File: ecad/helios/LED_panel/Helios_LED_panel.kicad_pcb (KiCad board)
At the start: 2 copper layers, 100 x 102.5 mm, 29 parts

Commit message: Layouts and polishes the LED panel
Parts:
- removed D17, D18: White 4000K 3W, FORT:OSRAM_Platinium_Dragon_Reflector
- removed the REF** at (197.5, 60.0)
- removed the REF** at (127.5, 60.0)
- removed the REF** at (162.5, 95.0)
- removed the REF** at (127.5, 130.0)
- removed the REF** at (197.5, 130.0)
- added REF**: Carclo_10740, FORT:Carclo_10740, F.Cu at (132.5, 72.5)
- added REF**: Carclo_10740, FORT:Carclo_10740, F.Cu at (182.5, 122.5)
- added REF**: Carclo_10740, FORT:Carclo_10740, F.Cu at (207.5, 122.5)
- added REF**: Carclo_10740, FORT:Carclo_10740, F.Cu at (132.5, 147.5)
- added REF**: Carclo_10740, FORT:Carclo_10740, F.Cu at (157.5, 147.5)
- added REF**: Carclo_10740, FORT:Carclo_10740, F.Cu at (182.5, 147.5)
- added REF**: Carclo_10740, FORT:Carclo_10740, F.Cu at (207.5, 147.5)
- added REF**: Carclo_10740, FORT:Carclo_10740, F.Cu at (207.5, 97.5)
- added REF**: MountingHole_3.2mm_M3_DIN965, Mounting_Holes:MountingHole_3.2mm_M3_DIN965, F.Cu at (195.0, 85.0)
- added REF**: MountingHole_3.2mm_M3_DIN965, Mounting_Holes:MountingHole_3.2mm_M3_DIN965, F.Cu at (145.0, 85.0)
- added REF**: MountingHole_3.2mm_M3_DIN965, Mounting_Holes:MountingHole_3.2mm_M3_DIN965, F.Cu at (145.0, 135.0)
- added REF**: Carclo_10740, FORT:Carclo_10740, F.Cu at (157.5, 72.5)
- added REF**: MountingHole_3.2mm_M3_DIN965, Mounting_Holes:MountingHole_3.2mm_M3_DIN965, F.Cu at (195.0, 135.0)
- added REF**: Carclo_10740, FORT:Carclo_10740, F.Cu at (182.5, 72.5)
- added REF**: Carclo_10740, FORT:Carclo_10740, F.Cu at (207.5, 72.5)
- added REF**: Carclo_10740, FORT:Carclo_10740, F.Cu at (132.5, 97.5)
- added REF**: Carclo_10740, FORT:Carclo_10740, F.Cu at (157.5, 97.5)
- added REF**: Carclo_10740, FORT:Carclo_10740, F.Cu at (182.5, 97.5)
- added REF**: Carclo_10740, FORT:Carclo_10740, F.Cu at (132.5, 122.5)
- added REF**: Carclo_10740, FORT:Carclo_10740, F.Cu at (157.5, 122.5)
- D1, D10, D11, D12, D15, D16, D2, D3, D4, D5, D6, D7, D8, D9: footprint FORT:OSRAM_Platinium_Dragon_Reflector -> FORT:OSRAM_Platinium_Dragon
- D13, D14: value NIR 850nm 3W -> White 4000K 3W; footprint FORT:OSRAM_Platinium_Dragon_Reflector -> FORT:OSRAM_Platinium_Dragon
- moved IR_A_GND1 145.9 mm to (163.2, 63.2)
- moved D6 117.3 mm to (157.5, 147.5), turned to 270 degrees
- moved D15 107.4 mm to (207.5, 147.3)
- moved IR_B_VCC1 100.6 mm to (182.5, 63.2)
- moved D12 86.1 mm to (182.5, 147.5), turned to 270 degrees
- moved VIS_GND1 79.6 mm to (126.8, 63.2)
- moved D14 73.8 mm to (132.5, 147.5), turned to 270 degrees
- moved IR_B_GND1 70.3 mm to (177.0, 63.2)
- moved D5 66.4 mm to (157.5, 122.5), turned to 270 degrees
- moved D9 62.5 mm to (207.5, 97.5)
- moved D7 55.2 mm to (182.5, 72.5), turned to 270 degrees
- moved IR_A_VCC1 54.0 mm to (157.5, 63.2)
- moved D13 50.0 mm to (132.5, 72.5), turned to 270 degrees
- moved D1 49.1 mm to (157.5, 72.5)
- moved D2 47.6 mm to (157.5, 97.5)
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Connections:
- D13 pad 2: Net-(D12-Pad1) -> Net-(D13-Pad2)
- D15 pad 2: Net-(D15-Pad2) -> Net-(D14-Pad1)
- D7 pad 2: Net-(D6-Pad1) -> Net-(D7-Pad2)
- D8 pad 2: Net-(D8-Pad2) -> Net-(D7-Pad1)
- IR_A_GND1 pad 1: Net-(D7-Pad1) -> Net-(D6-Pad1)
- IR_B_GND1 pad 1: Net-(D14-Pad1) -> Net-(D12-Pad1)
- IR_B_VCC1 pad 1: Net-(D8-Pad2) -> Net-(D7-Pad2)
- VIS_GND1 pad 1: Net-(D18-Pad1) -> Net-(D16-Pad1)
- VIS_VCC1 pad 1: Net-(D15-Pad2) -> Net-(D13-Pad2)
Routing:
- net Net-(D16-Pad1): track 0.00 -> 333.3 mm
- net Net-(D15-Pad1): track 0.00 -> 114.4 mm
- net Net-(D12-Pad1): track 0.00 -> 106.3 mm
- net Net-(D6-Pad1): track 0.00 -> 106.2 mm
- net Net-(D14-Pad1): track 0.00 -> 91.2 mm
- net Net-(D13-Pad1): track 0.00 -> 70.5 mm
- net Net-(D8-Pad1): track 0.00 -> 44.9 mm
- net Net-(D2-Pad1): track 0.00 -> 43.7 mm
- net Net-(D10-Pad1): track 0.00 -> 43.7 mm
- net Net-(D4-Pad1): track 0.00 -> 43.6 mm
- net Net-(D3-Pad1): track 0.00 -> 14.8 mm
- net Net-(D7-Pad1): track 0.00 -> 14.7 mm
- net Net-(D5-Pad1): track 0.00 -> 14.7 mm
- net Net-(D11-Pad1): track 0.00 -> 14.7 mm
- net Net-(D10-Pad2): track 0.00 -> 14.7 mm
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- added copper zone on F.Cu, net (none)
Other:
- board size 100 x 102.5 mm -> 100 x 100 mm
- net class Default: trace_width 0.25 -> 1.2

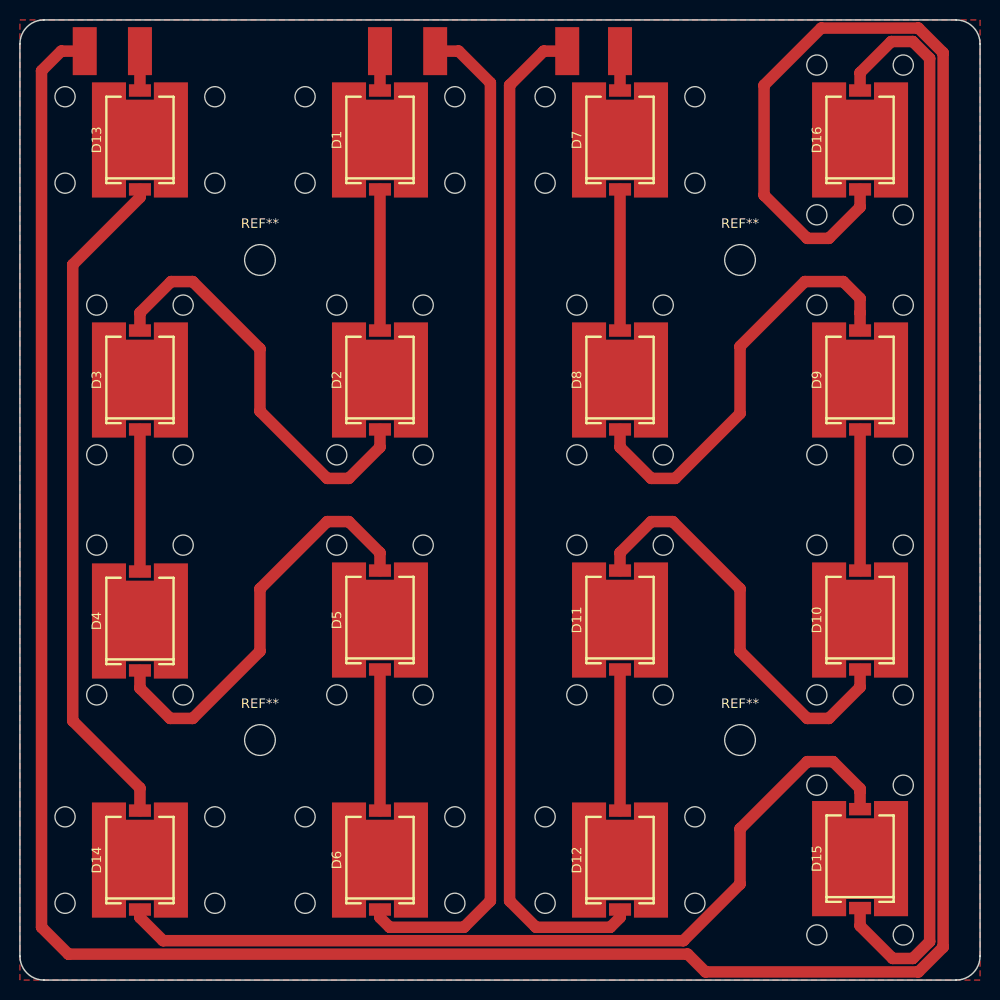
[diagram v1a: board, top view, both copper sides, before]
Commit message: Changes the holder for Platinium dragon
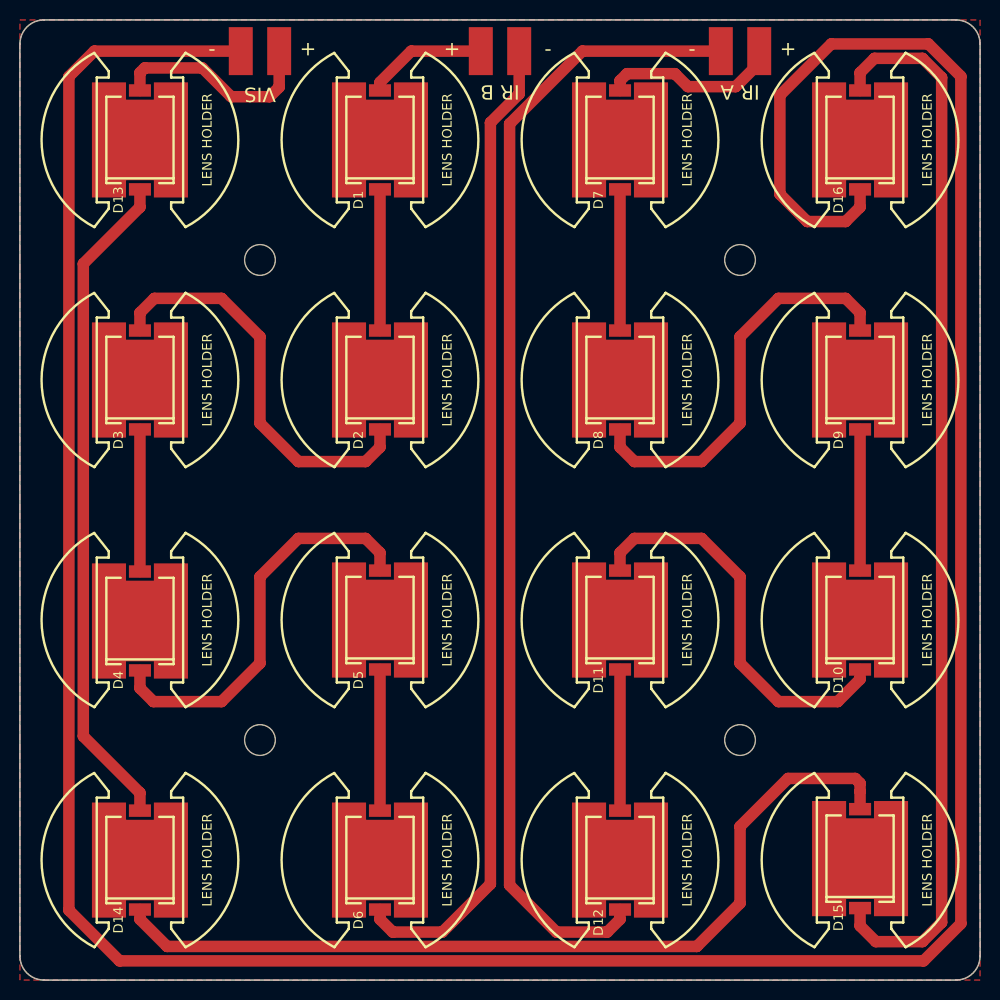
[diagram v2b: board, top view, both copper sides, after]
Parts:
- REF** (x16): footprint FORT:Carclo_10740 -> FORT:Carclo_10148
- moved VIS_GND1 16.2 mm to (143.0, 63.2)
- moved IR_B_GND1 16.0 mm to (193.0, 63.2)
- moved IR_B_VCC1 14.5 mm to (197.0, 63.2)
- moved VIS_VCC1 14.5 mm to (147.0, 63.2)
- moved IR_A_VCC1 10.5 mm to (168.0, 63.2)
- moved IR_A_GND1 8.75 mm to (172.0, 63.2)
- turned REF** to 90 degrees (x9)
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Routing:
- net Net-(D13-Pad2): track 4.10 -> 22.0 mm
- net Net-(D7-Pad2): track 4.10 -> 18.6 mm
- net Net-(D12-Pad1): track 106.3 -> 119.5 mm
- net Net-(D1-Pad2): track 4.10 -> 12.6 mm
- net Net-(D6-Pad1): track 106.2 -> 103.1 mm
- net Net-(D15-Pad1): track 114.4 -> 111.7 mm
- net Net-(D8-Pad1): track 44.9 -> 42.3 mm
- net Net-(D16-Pad1): track 333.3 -> 335.5 mm
- net Net-(D10-Pad1): track 43.7 -> 41.8 mm
- net Net-(D4-Pad1): track 43.6 -> 42.2 mm
- net Net-(D2-Pad1): track 43.7 -> 42.3 mm
- net Net-(D13-Pad1): track 70.5 -> 69.6 mm
- net Net-(D14-Pad1): track 91.2 -> 92.0 mm
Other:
- net class Default: clearance 0.2 -> 0.3
- rule trace_clearance: 0.2 -> 0.3
- board text added: "+"
- board text added: "-"
- board text added: "IR A"
- board text added: "IR B"
- board text added: "VIS"

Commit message: wip
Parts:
- D1, D10, D11, D12, D2, D3, D4, D5, D6, D7, D8, D9: value NIR 850nm 3W -> SFH 4235-Z
- D13, D14, D15, D16: value White 4000K 3W -> LSW W5SM
- moved D15 0.15 mm to (207.5, 147.5), turned to 180 degrees
- moved D4 0.10 mm to (132.5, 122.5), turned to 180 degrees
- turned D1 to 180 degrees
- turned D10 to 180 degrees
- turned D11 to 180 degrees
- turned D12 to 180 degrees
- turned D13 to 180 degrees
- turned D14 to 180 degrees
- turned D16 to 180 degrees
- turned D2 to 180 degrees
- turned D3 to 180 degrees
- turned D5 to 180 degrees
- turned D6 to 180 degrees
- turned D7 to 180 degrees
- turned D8 to 180 degrees
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
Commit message: Conforms orientation of components to IPC standards
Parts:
- turned D1 to 90 degrees
- turned D10 to 90 degrees
- turned D11 to 90 degrees
- turned D12 to 90 degrees
- turned D13 to 90 degrees
- turned D14 to 90 degrees
- turned D15 to 90 degrees
- turned D16 to 90 degrees
- turned D2 to 90 degrees
- turned D3 to 90 degrees
- turned D4 to 90 degrees
- turned D5 to 90 degrees
- turned D6 to 90 degrees
- turned D7 to 90 degrees
- turned D8 to 90 degrees
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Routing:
- net Net-(D16-Pad1): track 335.5 -> 0.00 mm
- net Net-(D16-Pad3): track 0.00 -> 244.5 mm
- net Net-(D13-Pad3): track 0.00 -> 219.3 mm
- net Net-(D7-Pad3): track 0.00 -> 126.6 mm
- net Net-(D12-Pad1): track 119.5 -> 0.00 mm
- net Net-(D15-Pad1): track 111.5 -> 0.00 mm
- net Net-(D15-Pad3): track 0.00 -> 92.0 mm
- net Net-(D14-Pad1): track 92.0 -> 0.00 mm
- net Net-(D14-Pad3): track 0.00 -> 69.6 mm
- net Net-(D13-Pad1): track 69.6 -> 0.00 mm
- net Net-(D3-Pad3): track 0.00 -> 42.3 mm
- net Net-(D2-Pad1): track 42.3 -> 0.00 mm
- net Net-(D9-Pad3): track 0.00 -> 42.3 mm
- net Net-(D8-Pad1): track 42.3 -> 0.00 mm
- net Net-(D5-Pad3): track 0.00 -> 42.2 mm
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
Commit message: wip
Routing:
- net Net-(D16-Pad1): track 0.00 -> 335.5 mm
- net Net-(D16-Pad3): track 244.5 -> 0.00 mm
- net Net-(D13-Pad3): track 219.3 -> 0.00 mm
- net Net-(D7-Pad3): track 126.6 -> 0.00 mm
- net Net-(D12-Pad1): track 0.00 -> 119.5 mm
- net Net-(D15-Pad1): track 0.00 -> 111.5 mm
- net Net-(D15-Pad3): track 92.0 -> 0.00 mm
- net Net-(D14-Pad1): track 0.00 -> 92.0 mm
- net Net-(D14-Pad3): track 69.6 -> 0.00 mm
- net Net-(D13-Pad1): track 0.00 -> 69.6 mm
- net Net-(D3-Pad3): track 42.3 -> 0.00 mm
- net Net-(D2-Pad1): track 0.00 -> 42.3 mm
- net Net-(D9-Pad3): track 42.3 -> 0.00 mm
- net Net-(D8-Pad1): track 0.00 -> 42.3 mm
- net Net-(D5-Pad3): track 42.2 -> 0.00 mm
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
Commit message: Modifies the LED panel to have board-to-wire connectors
Having wire directly soldered to the board is too much hazardous, has
a shortcut could appear if two wires touches the boards.
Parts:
- removed IR_A_GND1, IR_A_VCC1, IR_B_GND1, IR_B_VCC1, VIS_GND1, VIS_VCC1: Conn_01x01, Wire_Pads:SolderWirePad_single_SMD_5x10mm
- added J1: IR_A, FORT:009176002701106, F.Cu at (169.8, 62.9)
- added J2: IR_B, FORT:009176002701106, F.Cu at (195.0, 62.9)
- added J3: VIS, FORT:009176002701106, F.Cu at (145.0, 62.9)
- added REF**: Symbol_Attention_CopperTop_Small, Symbols:Symbol_Attention_CopperTop_Small, F.Cu at (174.2, 135.5)
- added REF***: OSHW-Logo2_9.8x8mm_SilkScreen, Symbols:OSHW-Logo2_9.8x8mm_SilkScreen, F.Cu at (195.2, 109.8)
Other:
- board text added: "CAUTION Hot Surface"
- board text added: "Helios LED Panel rev B"
- board text added: "© 2018 Alexandre Tuleu"

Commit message: Updates Helios Master 36V power Connector
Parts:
- added G***: LOGO, FORT:UNIL-LOGO_13.8x5.1mm, F.Cu at (207.7, 110.2)
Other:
- board text added: "© 2018 Université de Lausanne"
- board text removed: "© 2018 Alexandre Tuleu"
